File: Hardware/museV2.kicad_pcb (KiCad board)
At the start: 2 copper layers, 142.3 x 55.5 mm, 391 parts, among them P1 RCA_conn_x2, P10 -15V, P11 ~4, P13 ~5, P18 RX7, P19 3.3V, P20 TX6, P21 1.8V, P22 PSU_CTL, P23 GND, P3 3.5mm_conn_tip_switch, P31 P1, P32 L1.8_1, P33 L3.3_1, P34 P2, P35 L1.8_2, P36 L3.3_2, P37 P3, P38 L1.8_3, P39 L3.3_3, P4 3.5mm_conn_tip_switch, P40 P4, P41 L1.8_4, P42 L3.3_4, P43 +5V, P5 CONN_01X06, P6 CONN_02X14, P7 ~2, P8 +15V, P9 ~3, Q1 PMOS, Q2 BSS138, SW1 PWR_BTN, SW2 PAIR_BTN, U1 TPS65130, U10 PCM1863, U11 PCM1796, U12 NE5534, U13 NE5534, U14 NE5534, U15 NE5534, U16 NE5534, U17 NE5534, U18 EdisonConnector, U19 GTL2010, U2 LP38692, U20 GTL2010, U21 GTL2010, U22 PCA9685BS, U3 PLR135/T10, U4 POM-3535L-3-R, U5 POM-3535L-3-R, U6 PLT133/T10W, U7 POM-3535L-3-R, U8 POM-3535L-3-R, U9 PCM9211, X1 24.576 MHz

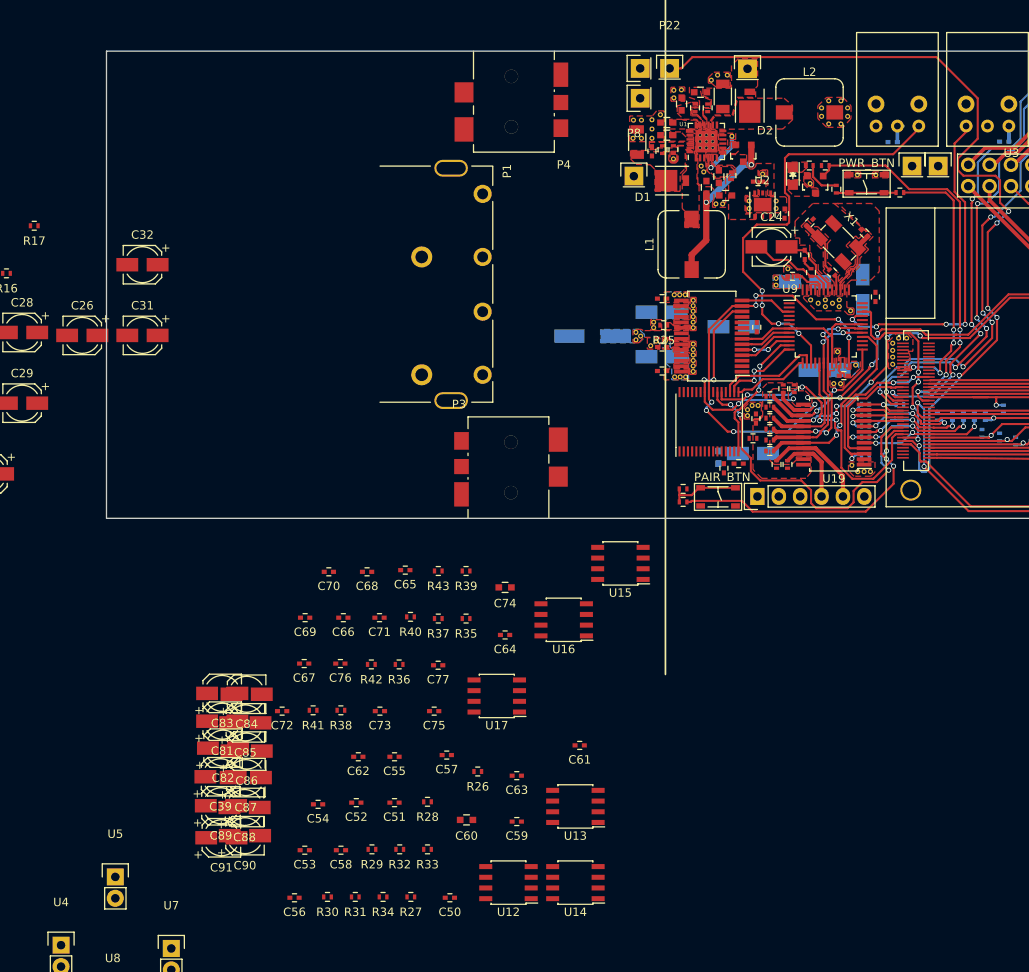
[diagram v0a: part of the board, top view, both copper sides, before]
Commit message: Continuing placement of op-amps
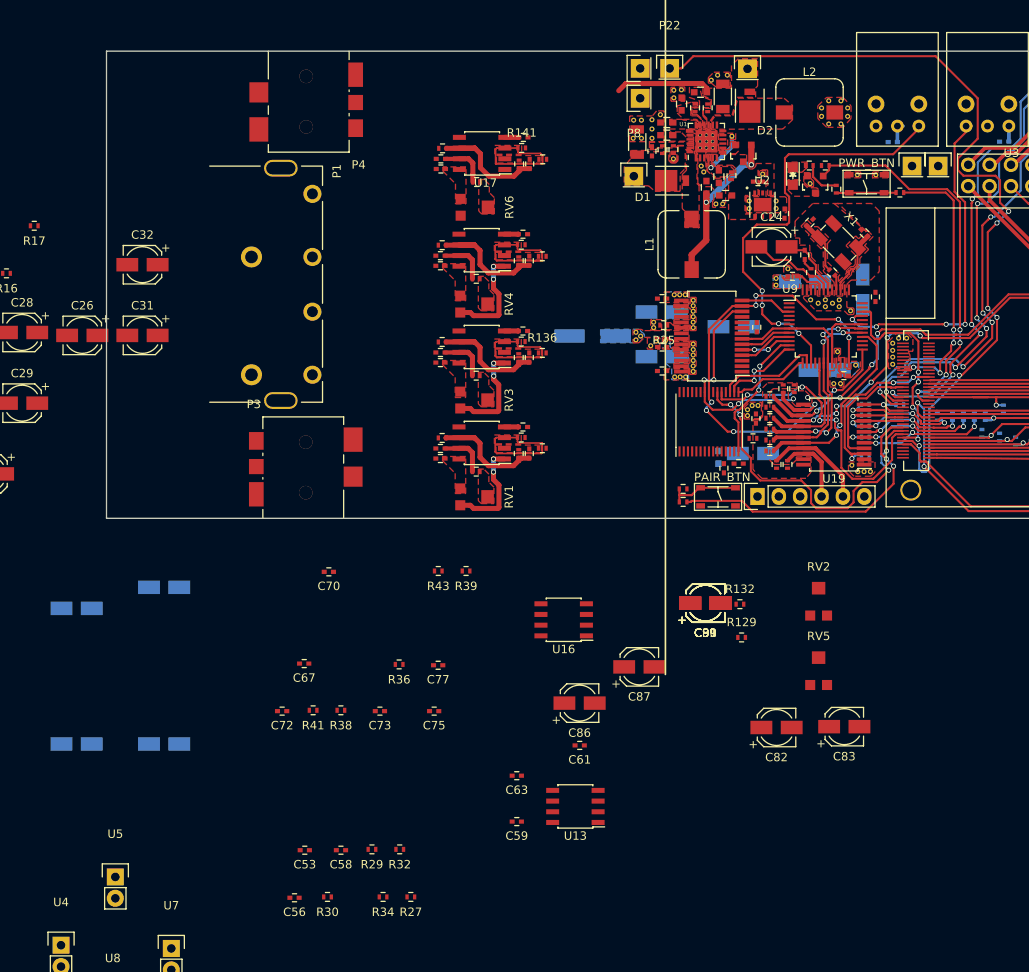
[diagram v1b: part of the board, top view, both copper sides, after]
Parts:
- added R129: 22K, Resistors_SMD:R_0402, F.Cu at (168.7, 165.2)
- added R130: 22K, Resistors_SMD:R_0402, F.Cu at (137.1, 134.1)
- added R131: 22K, Resistors_SMD:R_0402, F.Cu at (137.1, 122.5)
- added R132: 22K, Resistors_SMD:R_0402, F.Cu at (168.4, 161.2)
- added R133: 22K, Resistors_SMD:R_0402, F.Cu at (137.2, 111.0)
- added R134: 0, Resistors_SMD:R_0402, F.Cu at (145.0, 142.7)
- added R135: 0, Resistors_SMD:R_0402, F.Cu at (142.5, 141.4)
- added R136: 0, Resistors_SMD:R_0402, F.Cu at (145.0, 131.3)
- added R137: 0, Resistors_SMD:R_0402, F.Cu at (142.5, 130.0)
- added R138: 0, Resistors_SMD:R_0402, F.Cu at (145.0, 119.9)
- added R139: 0, Resistors_SMD:R_0402, F.Cu at (142.5, 118.5)
- added R140: 0, Resistors_SMD:R_0402, F.Cu at (145.0, 108.3)
- added R141: 0, Resistors_SMD:R_0402, F.Cu at (142.5, 107.0)
- added R7: 22K, Resistors_SMD:R_0402, F.Cu at (137.1, 145.4)
- added RV1: 100K, muse-v2-lib:TC33X-1, F.Cu at (137.0, 148.4)
- added RV2: 100K, muse-v2-lib:TC33X-1, F.Cu at (177.8, 160.8)
- added RV3: 100K, muse-v2-lib:TC33X-1, F.Cu at (137.0, 136.9)
- added RV4: 100K, muse-v2-lib:TC33X-1, F.Cu at (137.0, 125.5)
- added RV5: 100K, muse-v2-lib:TC33X-1, F.Cu at (177.8, 169.0)
- added RV6: 100K, muse-v2-lib:TC33X-1, F.Cu at (137.1, 114.0)
- C60, C74: footprint Capacitors_SMD:C_0603 -> Capacitors_SMD:C_0402
- C81, C84, C85, C88: moved to B.Cu
- moved C52 81.5 mm to (142.7, 105.8), turned to 0 degrees
- moved C54 78.1 mm to (132.9, 108.3)
- moved C83 74.0 mm to (180.8, 175.8)
- moved C51 69.2 mm to (142.7, 117.2), turned to 0 degrees
- moved R31 66.7 mm to (133.1, 130.1), turned to 0 degrees
- moved C82 65.8 mm to (172.8, 175.8)
- moved U14 64.6 mm to (137.8, 130.6)
- moved U17 64.5 mm to (137.8, 107.7)
- moved C91 63.9 mm to (164.3, 161.1)
- moved C89 62.4 mm to (164.3, 161.1)
- moved R42 62.0 mm to (142.2, 108.9), turned to 90 degrees
- moved C90 61.3 mm to (164.3, 161.1)
- moved C39 61.2 mm to (164.3, 161.1)
- moved C76 60.0 mm to (132.9, 109.5)
- moved C55 59.8 mm to (132.9, 119.8)
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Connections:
- C39 pad 1: -15V -> GND
- C39 pad 2: GND -> -15V
- C50 pad 2: /DAC/sheet57F8A4E6/ANALOG_OUT- -> Net-(C50-Pad2)
- C60 pad 2: /DAC/sheet57F8A4E6/ANALOG_OUT+ -> Net-(C60-Pad2)
- C64 pad 2: /DAC/sheet57F8A4E7/ANALOG_OUT- -> Net-(C64-Pad2)
- C74 pad 2: /DAC/sheet57F8A4E7/ANALOG_OUT+ -> Net-(C74-Pad2)
- C81 pad 1: -15V -> GND
- C81 pad 2: GND -> -15V
- C82 pad 1: -15V -> GND
- C82 pad 2: GND -> -15V
- C85 pad 1: +15V -> GND
- C85 pad 2: GND -> -15V
- C86 pad 1: -15V -> GND
- C86 pad 2: GND -> -15V
- C87 pad 1: -15V -> +15V
- C88 pad 1: -15V -> +15V
- C90 pad 1: +15V -> GND
- C90 pad 2: GND -> -15V
- R26 pad 2: /DAC/sheet57F8A4E6/ANALOG_OUT- -> Net-(C50-Pad2)
- R33 pad 2: /DAC/sheet57F8A4E6/ANALOG_OUT+ -> Net-(C60-Pad2)
- R35 pad 2: /DAC/sheet57F8A4E7/ANALOG_OUT- -> Net-(C64-Pad2)
- R42 pad 2: /DAC/sheet57F8A4E7/ANALOG_OUT+ -> Net-(C74-Pad2)
- U12 pad 1: (no net) -> Net-(RV1-Pad3)
- U12 pad 2: /DAC/sheet57F8A4E6/ANALOG_OUT- -> Net-(C50-Pad2)
- U12 pad 3: GND -> Net-(R135-Pad1)
- U12 pad 5: Net-(C57-Pad1) -> Net-(C57-Pad2)
- U12 pad 8: Net-(C57-Pad2) -> Net-(C57-Pad1)
- U13 pad 1: (no net) -> Net-(RV2-Pad3)
- U13 pad 5: Net-(C58-Pad1) -> Net-(C58-Pad2)
- U13 pad 8: Net-(C58-Pad2) -> Net-(C58-Pad1)
- U14 pad 1: (no net) -> Net-(RV3-Pad3)
- U14 pad 2: /DAC/sheet57F8A4E6/ANALOG_OUT+ -> Net-(C60-Pad2)
- U14 pad 3: GND -> Net-(R137-Pad1)
- U14 pad 5: Net-(C62-Pad1) -> Net-(C62-Pad2)
- U14 pad 8: Net-(C62-Pad2) -> Net-(C62-Pad1)
- U15 pad 1: (no net) -> Net-(RV4-Pad3)
- U15 pad 2: /DAC/sheet57F8A4E7/ANALOG_OUT- -> Net-(C64-Pad2)
- U15 pad 3: GND -> Net-(R139-Pad1)
- U15 pad 5: Net-(C71-Pad1) -> Net-(C71-Pad2)
- U15 pad 8: Net-(C71-Pad2) -> Net-(C71-Pad1)
- U16 pad 1: (no net) -> Net-(RV5-Pad3)
- U16 pad 5: Net-(C72-Pad1) -> Net-(C72-Pad2)
- U16 pad 8: Net-(C72-Pad2) -> Net-(C72-Pad1)
- U17 pad 1: (no net) -> Net-(RV6-Pad3)
- U17 pad 2: /DAC/sheet57F8A4E7/ANALOG_OUT+ -> Net-(C74-Pad2)
- U17 pad 3: GND -> Net-(R141-Pad1)
- U17 pad 5: Net-(C76-Pad1) -> Net-(C76-Pad2)
- U17 pad 8: Net-(C76-Pad2) -> Net-(C76-Pad1)
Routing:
- net +15V: track 0.00 -> 22.9 mm
- net -15V: track 0.00 -> 18.1 mm
- net Net-(C60-Pad1): track 0.00 -> 14.8 mm
- net Net-(C74-Pad1): track 0.00 -> 14.8 mm
- net Net-(C50-Pad1): track 0.00 -> 14.8 mm
- net Net-(C64-Pad1): track 0.00 -> 14.8 mm
- net Net-(R141-Pad1): track 0.00 -> 14.7 mm
- net Net-(R135-Pad1): track 0.00 -> 14.6 mm
- net Net-(R139-Pad1): track 0.00 -> 14.6 mm
- net Net-(R137-Pad1): track 0.00 -> 14.5 mm
- net Net-(RV1-Pad3): track 0.00 -> 12.1 mm, vias 0 -> 2
- net Net-(RV4-Pad3): track 0.00 -> 12.1 mm, vias 0 -> 2
- net Net-(RV3-Pad3): track 0.00 -> 11.9 mm, vias 0 -> 2
- added copper zone on F.Cu, net Net-(C50-Pad2)
- added copper zone on F.Cu, net Net-(C57-Pad1)
- added copper zone on F.Cu, net Net-(C60-Pad2)
- added copper zone on F.Cu, net Net-(C62-Pad1)
- added copper zone on F.Cu, net Net-(C64-Pad2)
- added copper zone on F.Cu, net Net-(C71-Pad1)
- added copper zone on F.Cu, net Net-(C74-Pad2)
- added copper zone on F.Cu, net Net-(C76-Pad1)
- added copper zone on F.Cu, net Net-(R130-Pad2)
- added copper zone on F.Cu, net Net-(R131-Pad2)
- added copper zone on F.Cu, net Net-(R133-Pad2)
- added copper zone on F.Cu, net Net-(R135-Pad1)
- added copper zone on F.Cu, net Net-(R137-Pad1)
- added copper zone on F.Cu, net Net-(R139-Pad1)
- added copper zone on F.Cu, net Net-(R141-Pad1)
- added copper zone on F.Cu, net Net-(R7-Pad2)
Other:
- net class +/-15v added: clearance 0.15, trace_width 0.6, via_dia 0.6, via_drill 0.4

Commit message: (Digital) board fixes
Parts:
- moved P13 89.2 mm to (164.3, 161.1)
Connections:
- C6 pad 1: +5V -> +5VSB
- Q1 pad 3: +5V -> +5VSB
- R5 pad 2: +5V -> +5VSB
- U1 pad 5: +5V -> +5VSB
- U1 pad 6: +5V -> +5VSB

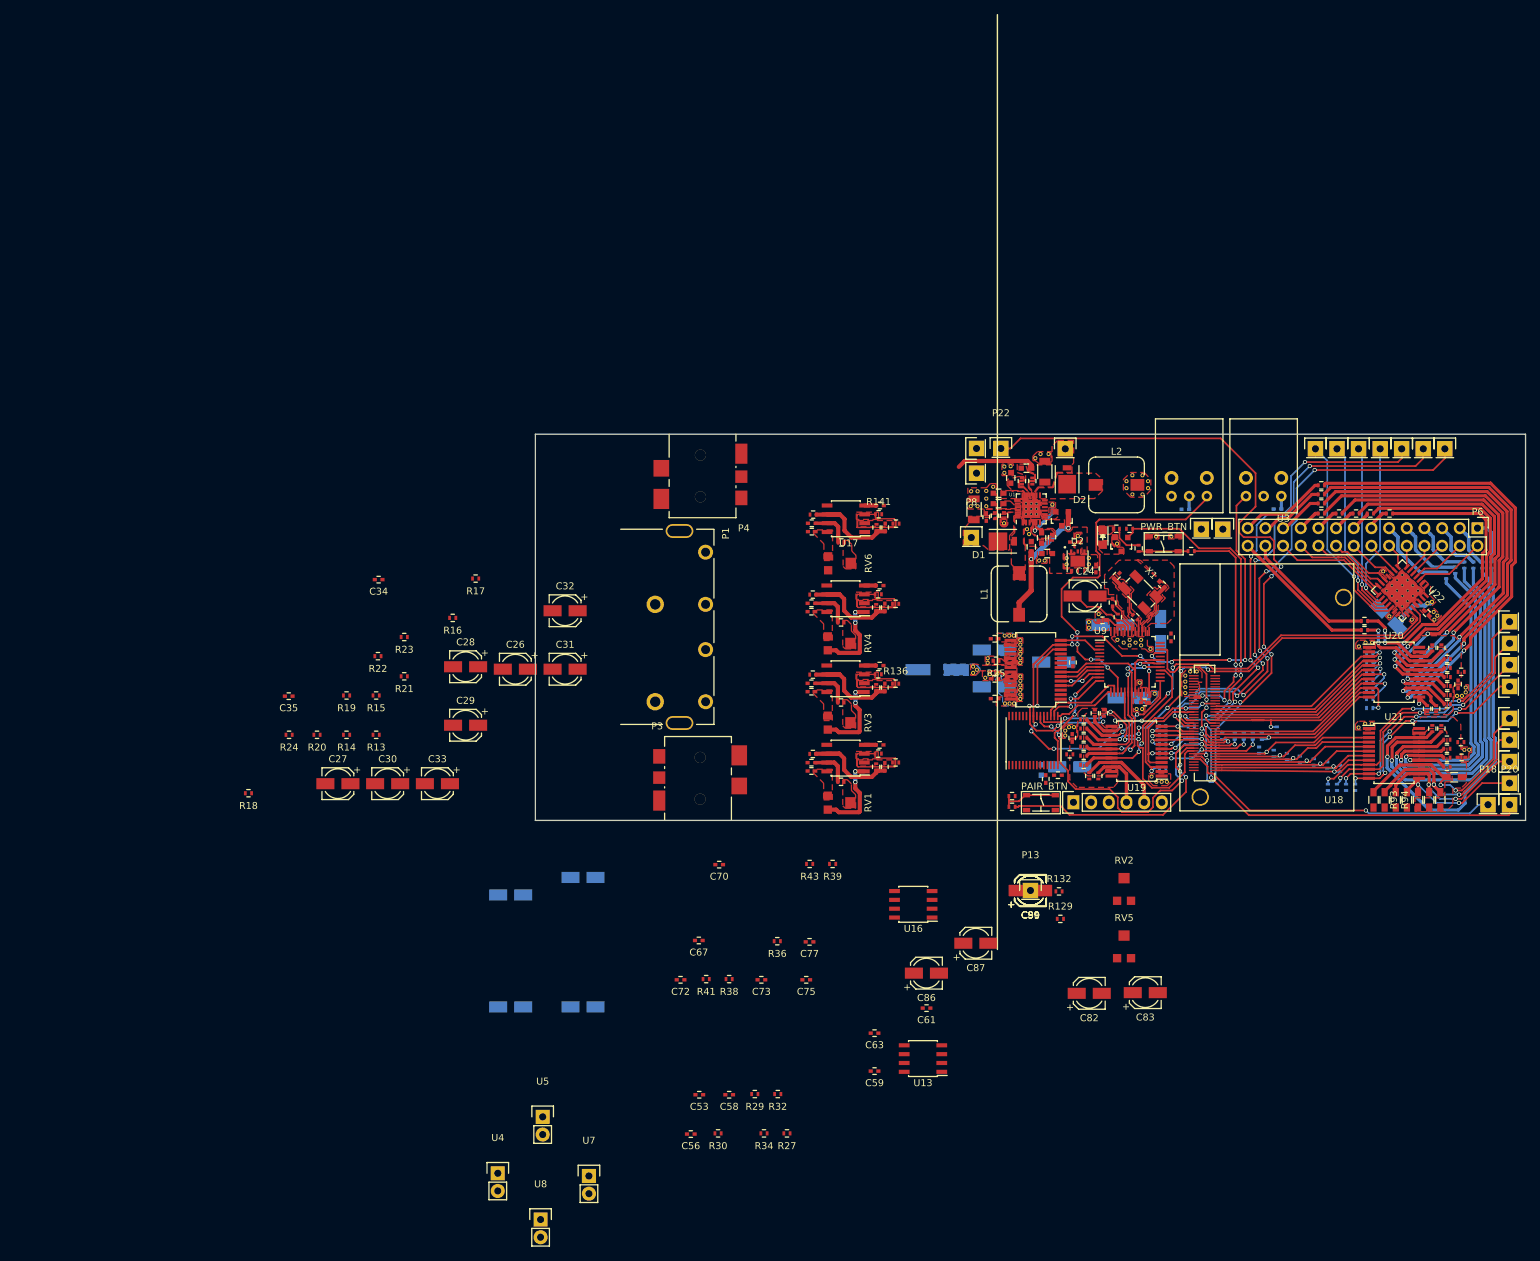
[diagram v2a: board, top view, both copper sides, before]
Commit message: Nearing end of op-amp placement
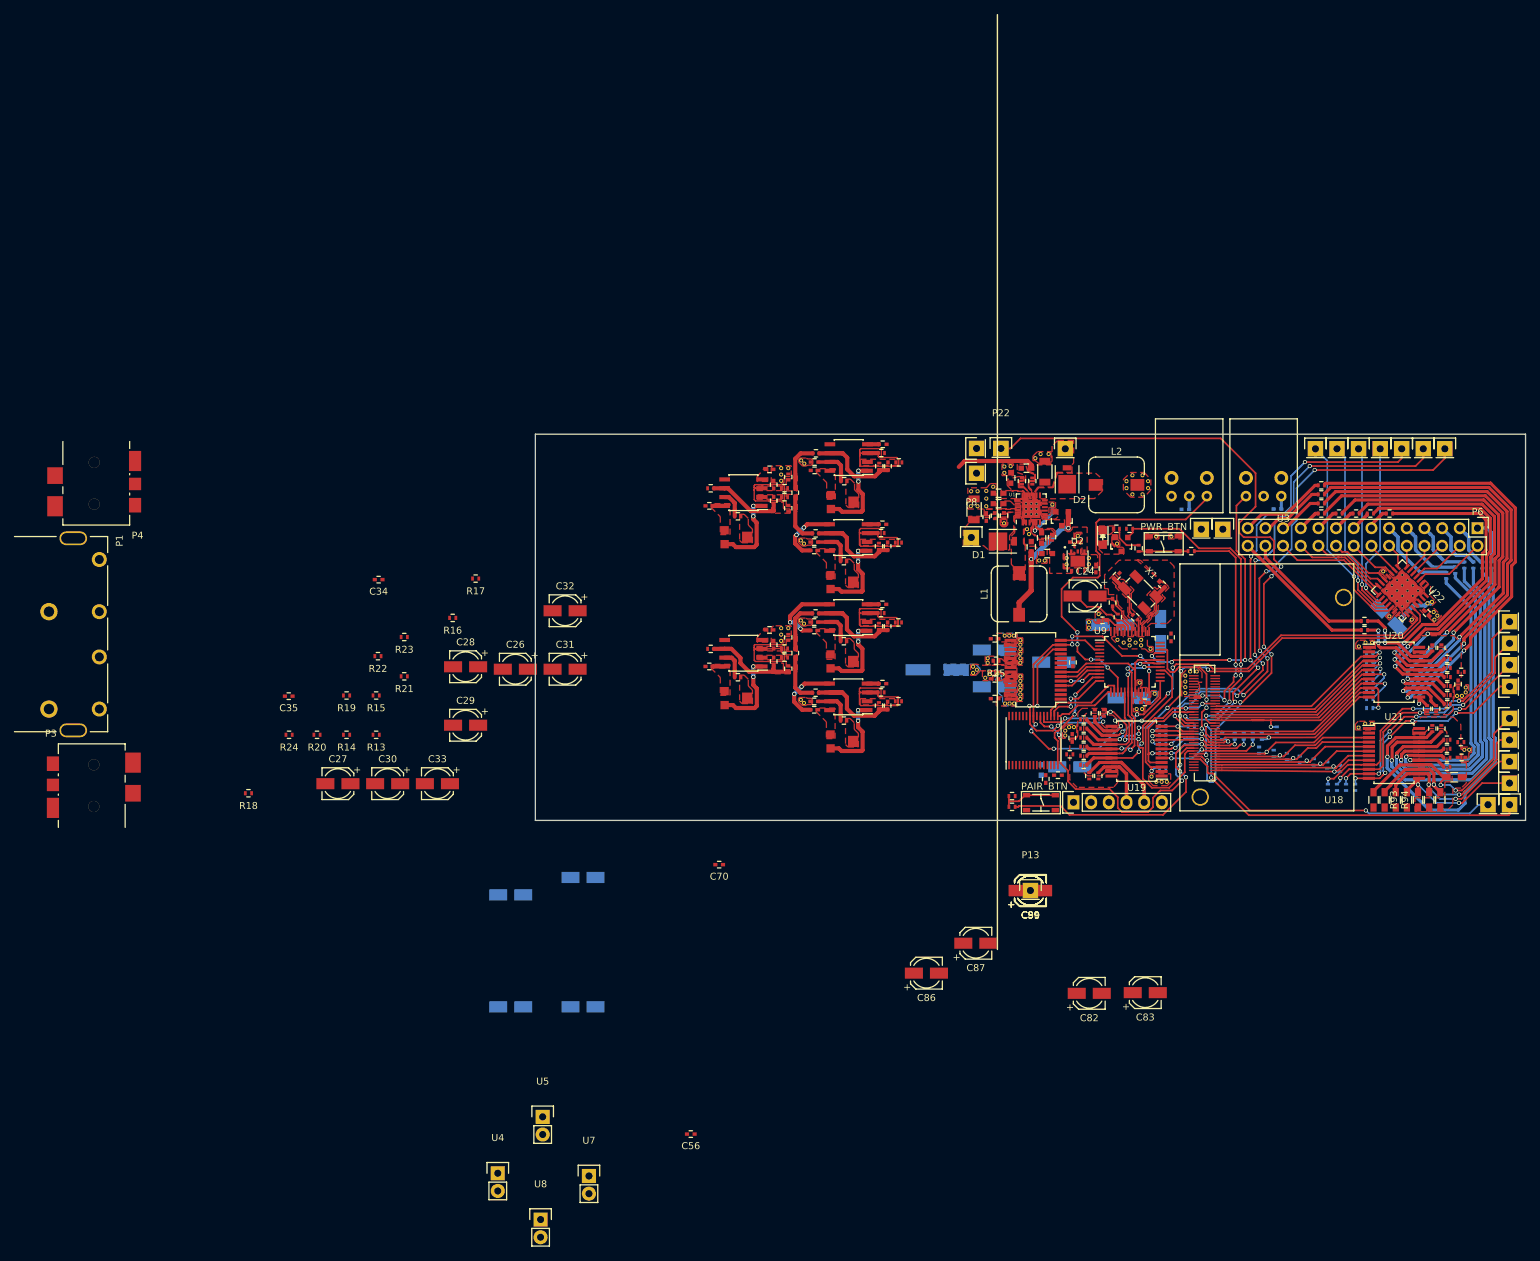
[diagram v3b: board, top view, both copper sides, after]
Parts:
- added REF**: VIA-0.3mm, muse-v2-lib:VIA-0.3mm, F.Cu at (128.5, 101.3)
- added REF**: VIA-0.3mm, muse-v2-lib:VIA-0.3mm, F.Cu at (131.8, 99.7)
- added REF**: VIA-0.3mm, muse-v2-lib:VIA-0.3mm, F.Cu at (131.3, 110.8)
- added REF**: VIA-0.3mm, muse-v2-lib:VIA-0.3mm, F.Cu at (131.8, 111.2)
- added REF**: VIA-0.3mm, muse-v2-lib:VIA-0.3mm, F.Cu at (131.3, 122.3)
- added REF**: VIA-0.3mm, muse-v2-lib:VIA-0.3mm, F.Cu at (131.8, 122.7)
- added REF**: VIA-0.3mm, muse-v2-lib:VIA-0.3mm, F.Cu at (131.3, 133.7)
- added REF**: VIA-0.3mm, muse-v2-lib:VIA-0.3mm, F.Cu at (131.8, 134.1)
- added REF**: VIA-0.3mm, muse-v2-lib:VIA-0.3mm, F.Cu at (128.5, 100.4)
- added REF**: VIA-0.3mm, muse-v2-lib:VIA-0.3mm, F.Cu at (128.5, 102.2)
- added REF**: VIA-0.3mm, muse-v2-lib:VIA-0.3mm, F.Cu at (129.6, 100.4)
- added REF**: VIA-0.3mm, muse-v2-lib:VIA-0.3mm, F.Cu at (128.5, 123.4)
- added REF**: VIA-0.3mm, muse-v2-lib:VIA-0.3mm, F.Cu at (129.6, 123.4)
- added REF**: VIA-0.3mm, muse-v2-lib:VIA-0.3mm, F.Cu at (128.5, 124.3)
- added REF**: VIA-0.3mm, muse-v2-lib:VIA-0.3mm, F.Cu at (128.5, 125.2)
- added REF**: VIA-0.3mm, muse-v2-lib:VIA-0.3mm, F.Cu at (131.4, 99.3)
- moved P1 87.1 mm to (30.5, 113.5)
- moved P3 87.1 mm to (29.8, 149.0)
- moved P4 87.1 mm to (29.8, 99.5)
- moved RV5 80.9 mm to (122.2, 110.3), turned to 270 degrees
- moved R41 71.4 mm to (129.0, 103.2), turned to 0 degrees
- moved R34 71.4 mm to (129.6, 124.7), turned to 90 degrees
- moved R132 71.0 mm to (122.3, 107.3)
- moved C75 70.0 mm to (130.6, 103.9), turned to 90 degrees
- moved R38 69.7 mm to (129.0, 104.5), turned to 0 degrees
- moved R30 69.6 mm to (118.4, 126.3), turned to 0 degrees
- moved C73 68.9 mm to (127.5, 105.0), turned to 90 degrees
- moved C67 68.5 mm to (126.8, 100.5), turned to 0 degrees
- moved C72 68.2 mm to (118.2, 105.8)
- moved C53 67.6 mm to (126.8, 123.6), turned to 0 degrees
- moved R27 66.8 mm to (129.6, 129.2), turned to 90 degrees
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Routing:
- net Net-(C63-Pad1): track 0.00 -> 18.7 mm
- net Net-(C77-Pad1): track 0.00 -> 15.3 mm
- net Net-(C59-Pad1): track 0.00 -> 13.4 mm
- net Net-(RV6-Pad3): track 0.00 -> 12.1 mm, vias 0 -> 2
- net Net-(RV2-Pad3): track 0.00 -> 12.1 mm, vias 0 -> 2
- net Net-(RV5-Pad3): track 0.00 -> 12.0 mm, vias 0 -> 2
- net Net-(C73-Pad1): track 0.00 -> 10.9 mm
- net Net-(C62-Pad2): track 0.00 -> 10.7 mm, vias 0 -> 2
- net Net-(C57-Pad2): track 0.00 -> 9.63 mm, vias 0 -> 2
- net Net-(C71-Pad2): track 0.00 -> 9.31 mm, vias 0 -> 2
- net +15V: track 22.9 -> 30.6 mm
- net Net-(C61-Pad2): track 0.00 -> 7.21 mm
- net Net-(C61-Pad1): track 0.00 -> 7.20 mm
- net Net-(C75-Pad1): track 0.00 -> 7.17 mm
- net Net-(C75-Pad2): track 0.00 -> 7.17 mm
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- added copper zone on F.Cu, net Net-(C58-Pad1)
- added copper zone on F.Cu, net Net-(C59-Pad1)
- added copper zone on F.Cu, net Net-(C59-Pad2)
- added copper zone on F.Cu, net Net-(C61-Pad1)
- added copper zone on F.Cu, net Net-(C61-Pad2)
- added copper zone on F.Cu, net Net-(C63-Pad1)
- added copper zone on F.Cu, net Net-(C72-Pad1)
- added copper zone on F.Cu, net Net-(C73-Pad1)
- added copper zone on F.Cu, net Net-(C73-Pad2)
- added copper zone on F.Cu, net Net-(C75-Pad1)
- added copper zone on F.Cu, net Net-(C75-Pad2)
- added copper zone on F.Cu, net Net-(C77-Pad1)
- added copper zone on F.Cu, net Net-(R129-Pad2)
- added copper zone on F.Cu, net Net-(R132-Pad2)
- removed copper zone on F.Cu, net Net-(R135-Pad1)
- removed copper zone on F.Cu, net Net-(R137-Pad1)
- removed copper zone on F.Cu, net Net-(R139-Pad1)
- removed copper zone on F.Cu, net Net-(R141-Pad1)
